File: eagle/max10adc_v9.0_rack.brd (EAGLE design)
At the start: 98 x 112 mm, 193 parts, among them IC1 MAX19506, IC2 MAX19506, J1 MOLEX_BNC_73100-0105, J2 MOLEX_BNC_73100-0105, J3 MOLEX_BNC_73100-0105, J4 MOLEX_BNC_73100-0105, K1 AQY21SOP, K2 AQY21SOP, K3 AQY21SOP, K4 AQY21SOP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

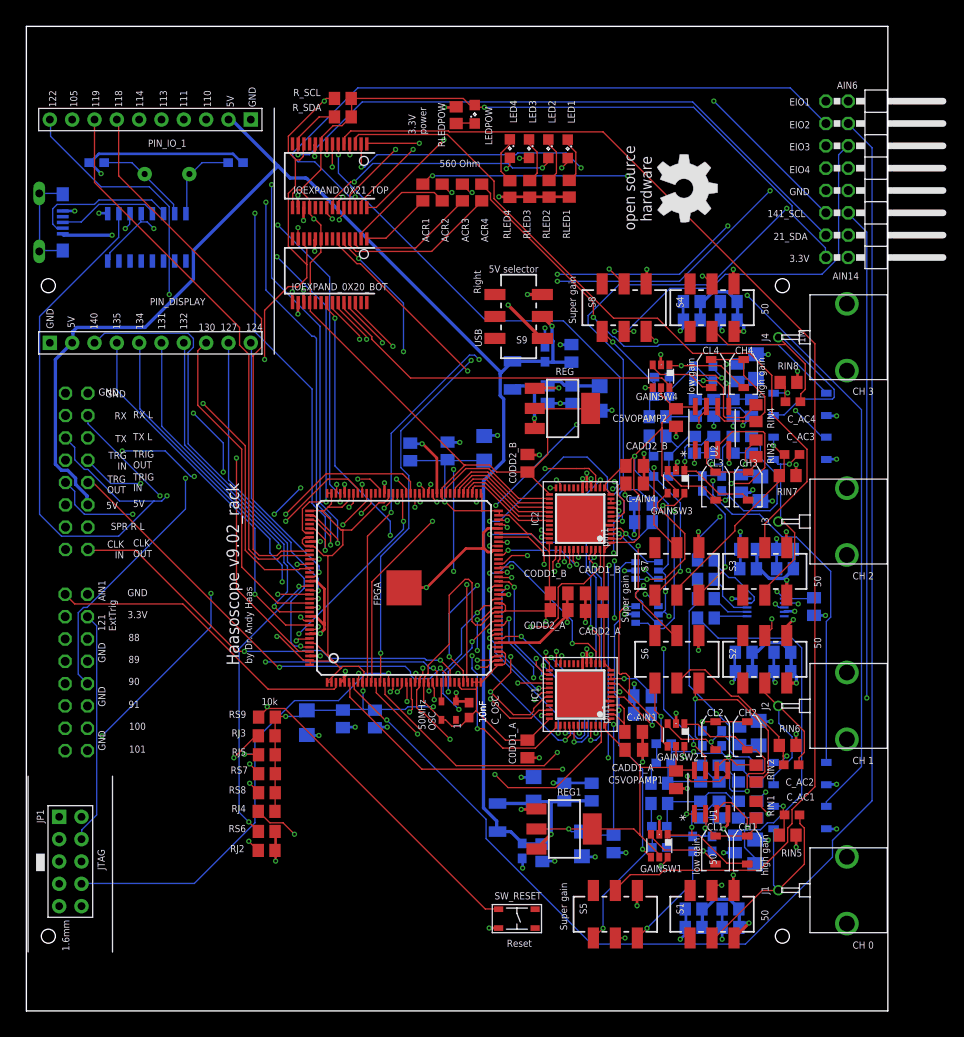
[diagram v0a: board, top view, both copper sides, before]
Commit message: use max 4416EUA, which is available
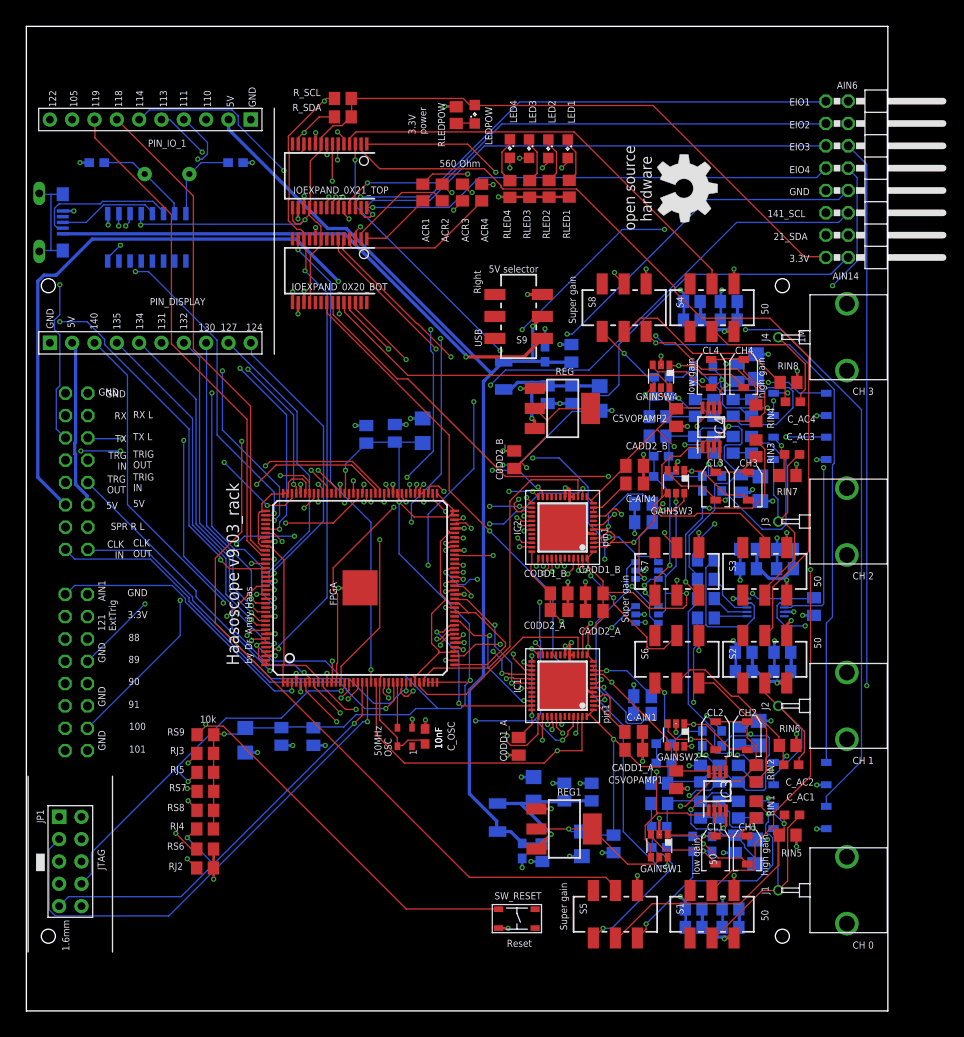
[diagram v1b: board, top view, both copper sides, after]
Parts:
- removed U1, U2: MAX4416ESA, LMH6724:M08A
- added IC3, IC4: MAX4416EUA+, SamacSys_Parts:SOP65P490X110-8N
- moved CG13 7.28 mm to (17.0, 13.2)
- moved CG14 7.28 mm to (12.9, 12.8)
- moved CG15 7.28 mm to (20.6, 13.2)
- moved CP6 7.28 mm to (33.1, 48.0)
- moved RJ2 7.28 mm to (8.33, -1.74)
- moved RJ3 7.28 mm to (8.34, 11.3)
- moved RJ4 7.28 mm to (8.33, 2.70)
- moved RJ5 7.28 mm to (8.36, 9.14)
- moved RS6 7.28 mm to (8.34, 0.42)
- moved RS7 7.28 mm to (8.37, 6.98)
- moved RS8 7.28 mm to (8.36, 4.82)
- moved RS9 7.28 mm to (8.37, 13.4)
- moved CV12 6.32 mm to (29.9, 47.7)
- moved C_OSC 5.83 mm to (33.4, 13.2)
- moved OSC 5.83 mm to (31.0, 13.2)
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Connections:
- net GND: now also IC3.4, IC4.4; no longer U1.4, U2.4
- net INA1: now also IC3.1; no longer U1.1
- net INA2: now also IC4.1; no longer U2.1
- net INAMINUS1: now also IC3.2; no longer U1.2
- net INAMINUS2: now also IC4.2; no longer U2.2
- net INB1: now also IC3.7; no longer U1.7
- net INB2: now also IC4.7; no longer U2.7
- net INBMINUS1: now also IC3.6; no longer U1.6
- net INBMINUS2: now also IC4.6; no longer U2.6
- net OFFSET1: now also IC3.3; no longer U1.3
- net OFFSET2: now also IC3.5; no longer U1.5
- net OFFSET3: now also IC4.3; no longer U2.3
- net OFFSET4: now also IC4.5; no longer U2.5
- net VCCA: now also IC3.8, IC4.8; no longer U1.8, U2.8
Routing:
- net +3V3: track 439.0 -> 517.1 mm, vias 11 -> 14
- net GND: track 266.5 -> 202.7 mm, vias 99 -> 106
- net A12: track 129.6 -> 90.2 mm, vias 2 -> 4
- net A10: track 94.4 -> 133.1 mm, vias 4 -> 2
- net A8: track 102.6 -> 138.6 mm, vias 4 -> 2
- net E_21_B0: track 159.8 -> 127.4 mm
- net A6: track 128.6 -> 156.4 mm
- net SERIALFROMRIGHT_TX_93: track 97.0 -> 69.4 mm, vias 2 -> 5
- net 5VINFROMRIGHT: track 64.2 -> 88.7 mm, vias 1 -> 2
- net CLKINFROMRIGHT_26: track 71.0 -> 47.6 mm, vias 2 -> 1
- net E_21_B4: track 144.5 -> 124.7 mm, vias 0 -> 2
- net IO_100: track 60.0 -> 40.2 mm, vias 3 -> 2
- net E_IO_2: track 76.0 -> 57.9 mm
- net IO_CLK_89: track 58.2 -> 40.2 mm, vias 1 -> 2
- net A7: track 159.1 -> 142.2 mm, vias 1 -> 2
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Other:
- board text added: "Haasoscope v9.03_rack"
- board text removed: "Haasoscope v9.02_rack"

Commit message: routed v9.10 6layer rack
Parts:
- moved SW_RESET 36.0 mm to (7.80, -8.50)
- moved REG 25.5 mm to (24.0, 55.5)
- moved CP2 25.2 mm to (22.3, 55.1)
- moved CP1 24.2 mm to (26.1, 55.1)
- moved CP5 23.5 mm to (30.2, 56.7)
- moved C_5V_10NF 20.0 mm to (31.0, 68.7)
- moved CP11 19.7 mm to (34.4, 68.8)
- moved C_5V_10NF1 17.8 mm to (30.4, -10.8), flipped to the top
- moved CP3 17.5 mm to (33.3, -5.20), flipped to the top, turned to 270 degrees
- moved REG1 17.3 mm to (40.2, -12.1)
- moved CP8 17.3 mm to (39.7, -4.90), flipped to the top, turned to 270 degrees
- moved CP7 17.1 mm to (36.8, -4.90), flipped to the top, turned to 270 degrees
- moved CP10 17.0 mm to (33.7, -11.0), flipped to the top
- moved L1 15.0 mm to (30.3, 63.3)
- moved L2 14.9 mm to (30.6, -6.00), flipped to the top
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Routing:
- net +3V3: track 517.1 -> 439.4 mm, vias 14 -> 10
- net GND: track 202.7 -> 133.7 mm, vias 106 -> 138
- net A6: track 156.4 -> 103.0 mm, vias 1 -> 2
- net A14: track 91.7 -> 134.9 mm, vias 2 -> 1
- net A8: track 138.6 -> 99.3 mm
- net IO_113: track 55.0 -> 89.4 mm, vias 3 -> 1
- net E_21_B1: track 95.6 -> 129.7 mm
- net A10: track 133.1 -> 99.1 mm
- net L120_SYNC: track 61.2 -> 91.8 mm, vias 4 -> 3
- net E_21_B0: track 127.4 -> 101.2 mm, vias 2 -> 3
- net VCCA: track 155.2 -> 180.8 mm, vias 7 -> 2
- net 5VINFROMRIGHT: track 88.7 -> 63.2 mm
- net E_21_B4: track 124.7 -> 99.4 mm
- net L135: track 39.7 -> 61.1 mm
- net LOW_24: track 48.5 -> 68.8 mm
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- added copper zone on layer 16, net GND
- added copper zone on layer 4, net GND
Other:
- board text added: "Haasoscope v9.10_rack_6layer"
- board text removed: "Haasoscope v9.03_rack"
